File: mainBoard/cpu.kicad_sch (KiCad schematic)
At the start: 11 parts

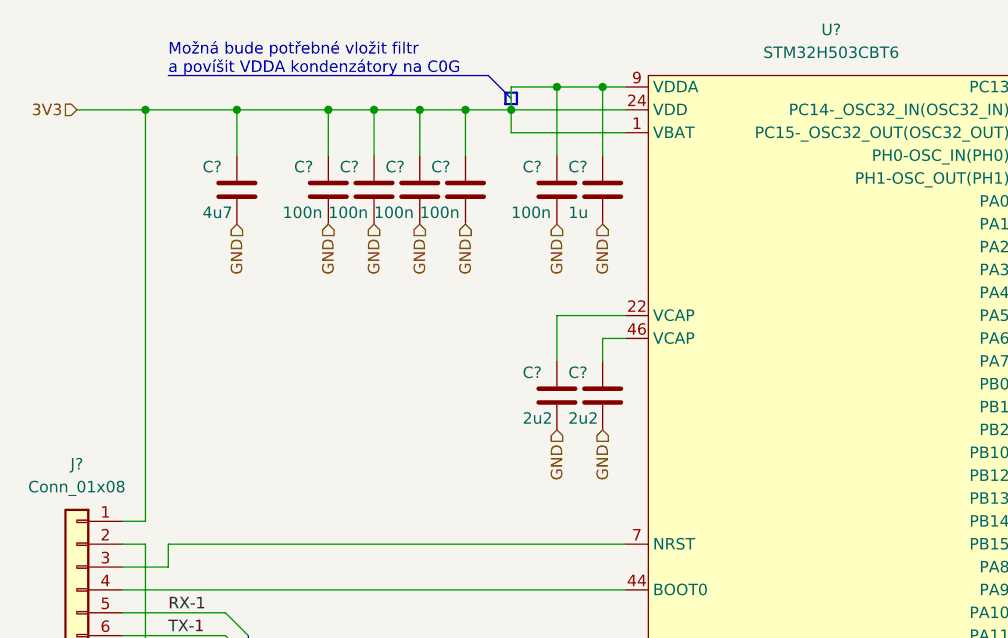
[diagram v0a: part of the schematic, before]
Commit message: LEDky, měření napájení, připojení DRV atd.
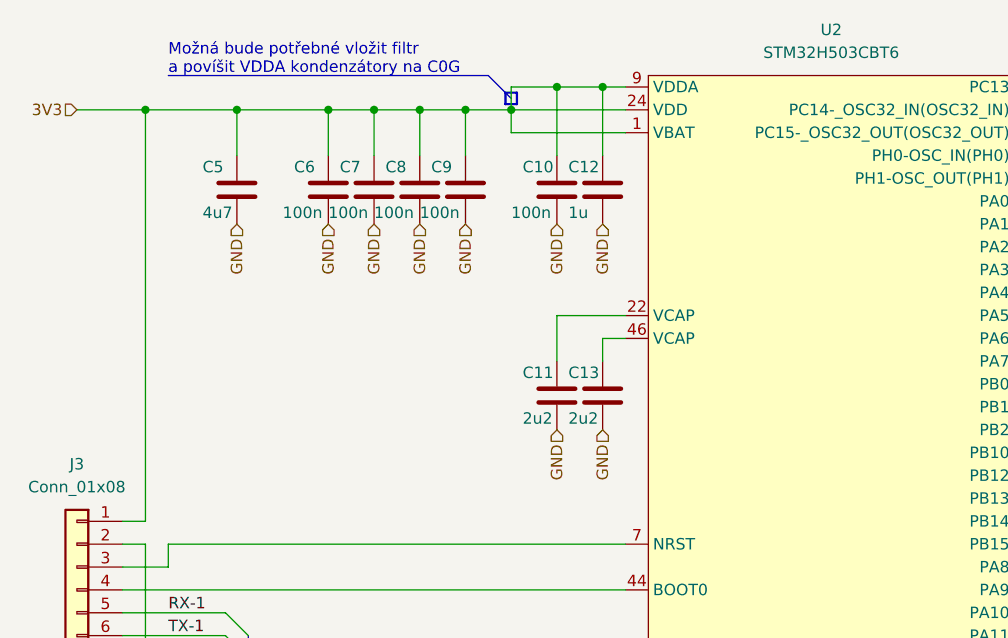
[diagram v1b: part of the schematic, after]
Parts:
- gave numbers to parts that had none: 11

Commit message: Pouzdra
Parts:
- J3: footprint (none) -> Connector_PinHeader_1.00mm:PinHeader_1x08_P1.00mm_Vertical
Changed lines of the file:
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@@
       (effects (font (size 1.27 1.27)))
     )
-    (property "Footprint" "" (at 63.5 100.33 0)
+    (property "Footprint" "Connector_PinHeader_1.00mm:PinHeader_1x08_P1.00mm_Vertical" (at 63.5 100.33 0)
       (effects (font (size 1.27 1.27)) hide)
     )

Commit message: test-pointy a zdvojení konektorů
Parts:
- J3: footprint Connector_PinHeader_1.00mm:PinHeader_1x08_P1.00mm_Vertical -> Connector_JST:JST_XH_B8B-XH-AM_1x08_P2.50mm_Vertical
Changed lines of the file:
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@@
       (effects (font (size 1.27 1.27)))
     )
-    (property "Footprint" "Connector_PinHeader_1.00mm:PinHeader_1x08_P1.00mm_Vertical" (at 63.5 100.33 0)
+    (property "Footprint" "Connector_JST:JST_XH_B8B-XH-AM_1x08_P2.50mm_Vertical" (at 63.5 100.33 0)
       (effects (font (size 1.27 1.27)) hide)
     )

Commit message: WIP
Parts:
- removed J3: Conn_01x08, Connector_JST:JST_XH_B8B-XH-AM_1x08_P2.50mm_Vertical, symbol Connector_Generic:Conn_01x08
- added J10: Conn_02x07_Odd_Even, Connector_PinHeader_1.27mm:PinHeader_2x07_P1.27mm_Vertical_SMD, symbol Connector_Generic:Conn_02x07_Odd_Even
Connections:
- net RX-1: now also J10.13 (Pin_13)
- net SWCLK: now also J10.6 (Pin_6)
- net SWDIO: now also J10.4 (Pin_4)
- net TX-1: now also J10.14 (Pin_14)
- net VDD: now also J10.3 (Pin_3)
- net VSS: now also J10.5 (Pin_5), J10.7 (Pin_7)
- net at U2.7 (NRST): now also J10.12 (Pin_12)
- no-connect marks 0 -> 7
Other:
- moved on the sheet: C10, C11, C12, C13, C5, C6, C7, C8, C9, U2

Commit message: WIP
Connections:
- net DRV-IN1 renamed DRV.IN1
- net DRV-IN2 renamed DRV.IN2
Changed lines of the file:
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@@
 (kicad_sch (version 20230121) (generator eeschema)
   (paper "A4")
+  (junction (at 121.92 43.18) (diameter 0) (color 0 0 0 0)
+  )
   (junction (at 91.44 45.72) (diameter 0) (color 0 0 0 0)
   )
@@
   )
   (junction (at 111.76 45.72) (diameter 0) (color 0 0 0 0)
-  )
-  (junction (at 121.92 43.18) (diameter 0) (color 0 0 0 0)
   )
   (junction (at 106.68 45.72) (diameter 0) (color 0 0 0 0)
@@
     (stroke (width 0) (type default))
   )
-  (bus_entry (at 187.96 93.98) (size 2.54 -2.54)
+  (bus_entry (at 190.5 91.44) (size -2.54 2.54)
     (stroke (width 0) (type default))
   )
@@
     (stroke (width 0) (type default))
   )
+  (wire (pts (xy 170.18 116.84) (xy 196.85 116.84))
+    (stroke (width 0) (type default))
+  )
+  (wire (pts (xy 170.18 109.22) (xy 187.96 109.22))
+    (stroke (width 0) (type default))
+  )
   (bus (pts (xy 190.5 93.98) (xy 190.5 91.44))
     (stroke (width 0) (type default))
@@
     (stroke (width 0) (type default))
   )
-  (wire (pts (xy 170.18 106.68) (xy 187.96 106.68))
-    (stroke (width 0) (type default))
-  )
   (wire (pts (xy 124.46 48.26) (xy 111.76 48.26))
     (stroke (width 0) (type default))
@@
     (stroke (width 0) (type default))
   )
+  (wire (pts (xy 170.18 73.66) (xy 207.01 73.66))
+    (stroke (width 0) (type default))
+  )
   (wire (pts (xy 116.84 68.58) (xy 124.46 68.58))
     (stroke (width 0) (type default))
   )
+  (wire (pts (xy 170.18 114.3) (xy 196.85 114.3))
+    (stroke (width 0) (type default))
+  )
   (bus (pts (xy 190.5 43.18) (xy 190.5 40.64))
     (stroke (width 0) (type default))
@@
     (stroke (width 0) (type default))
   )
-  (wire (pts (xy 170.18 116.84) (xy 196.85 116.84))
+  (wire (pts (xy 170.18 121.92) (xy 196.85 121.92))
+    (stroke (width 0) (type default))
+  )
+  (wire (pts (xy 121.92 43.18) (xy 124.46 43.18))
     (stroke (width 0) (type default))
   )
@@
     (stroke (width 0) (type default))
   )
-  (wire (pts (xy 170.18 127) (xy 201.93 127))
-    (stroke (width 0) (type default))
-  )
   (bus (pts (xy 199.39 50.8) (xy 207.01 50.8))
     (stroke (width 0) (type default))
   )
   (wire (pts (xy 60.96 96.52) (xy 69.85 96.52))
-    (stroke (width 0) (type default))
-  )
-  (wire (pts (xy 207.01 73.66) (xy 170.18 73.66))
-    (stroke (width 0) (type default))
-  )
-  (wire (pts (xy 170.18 119.38) (xy 196.85 119.38))
     (stroke (width 0) (type default))
   )
@@
     (stroke (width 0) (type default))
   )
+  (wire (pts (xy 170.18 127) (xy 201.93 127))
+    (stroke (width 0) (type default))
+  )
   (bus (pts (xy 190.5 43.18) (xy 190.5 78.74))
     (stroke (width 0) (type default))
@@
     (stroke (width 0) (type default))
   )
+  (wire (pts (xy 170.18 106.68) (xy 187.96 106.68))
+    (stroke (width 0) (type default))
+  )
+  (wire (pts (xy 170.18 119.38) (xy 196.85 119.38))
+    (stroke (width 0) (type default))
+  )
+  (wire (pts (xy 170.18 66.04) (xy 201.93 66.04))
+    (stroke (width 0) (type default))
+  )
   (wire (pts (xy 170.18 124.46) (xy 201.93 124.46))
     (stroke (width 0) (type default))
   )
-  (wire (pts (xy 170.18 114.3) (xy 196.85 114.3))
-    (stroke (width 0) (type default))
-  )
-  (wire (pts (xy 170.18 66.04) (xy 201.93 66.04))
-    (stroke (width 0) (type default))
-  )
-  (wire (pts (xy 121.92 43.18) (xy 124.46 43.18))
-    (stroke (width 0) (type default))
-  )
   (wire (pts (xy 63.5 45.72) (xy 67.31 45.72))
+    (stroke (width 0) (type default))
+  )
+  (bus (pts (xy 190.5 88.9) (xy 207.01 88.9))
     (stroke (width 0) (type default))
   )
@@
     (stroke (width 0) (type default))
   )
-  (wire (pts (xy 170.18 109.22) (xy 187.96 109.22))
-    (stroke (width 0) (type default))
-  )
   (wire (pts (xy 67.31 86.36) (xy 67.31 88.9))
     (stroke (width 0) (type default))
@@
     (stroke (width 0) (type default))
   )
-  (bus (pts (xy 190.5 88.9) (xy 207.01 88.9))
-    (stroke (width 0) (type default))
-  )
   (bus (pts (xy 199.39 114.3) (xy 199.39 116.84))
     (stroke (width 0) (type default))
@@
   )
   (bus (pts (xy 204.47 121.92) (xy 204.47 124.46))
-    (stroke (width 0) (type default))
-  )
-  (wire (pts (xy 170.18 121.92) (xy 196.85 121.92))
     (stroke (width 0) (type default))
   )
@@
     (effects (font (size 1.27 1.27)) (justify left bottom))
   )
-  (label "RX-2" (at 170.18 93.98 0) (fields_autoplaced)
+  (label "RX-2" (at 171.45 93.98 0) (fields_autoplaced)
     (effects (font (size 1.27 1.27)) (justify left bottom))
   )
@@
     (effects (font (size 1.27 1.27)) (justify left bottom))
   )
-  (label "DRV-IN1" (at 170.18 127 0) (fields_autoplaced)
+  (label "DRV.IN1" (at 170.18 127 0) (fields_autoplaced)
     (effects (font (size 1.27 1.27)) (justify left bottom))
   )
@@
     (effects (font (size 1.27 1.27)) (justify left bottom))
   )
-  (label "TX-2" (at 170.18 96.52 0) (fields_autoplaced)
+  (label "TX-2" (at 171.45 96.52 0) (fields_autoplaced)
     (effects (font (size 1.27 1.27)) (justify left bottom))
   )
@@
     (effects (font (size 1.27 1.27)) (justify left bottom))
   )
-  (label "DRV-IN2" (at 170.18 124.46 0) (fields_autoplaced)
-    (effects (font (size 1.27 1.27)) (justify left bottom))
-  )
+  (label "DRV.IN2" (at 170.18 124.46 0) (fields_autoplaced)
+    (effects (font (size 1.27 1.27)) (justify left bottom))
+  )

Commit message: ERC
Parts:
- removed U2: STM32H503CBT6, Package_QFP:LQFP-48-1EP_7x7mm_P0.5mm_EP3.6x3.6mm, symbol Robotarna_KiCad_Library:STM32H503CBT6
- added U2: STM32H503CBT6, Package_QFP:LQFP-48-1EP_7x7mm_P0.5mm_EP3.6x3.6mm, symbol RKL-STM:STM32H503CBT6
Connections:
- net DRV.IN1: now also U2.43 (PB7)
- net DRV.IN2: now also U2.42 (PB6)
- net MEŘENÍ-NAPÁJENÍ: now also U2.17 (PA7)
- net RX-1: now also U2.32 (PA11)
- net SWCLK: now also U2.37 (PA14(JTCK/SWCLK))
- net SWDIO: now also U2.34 (PA13(JTMS/SWDIO))
- net TX-1: now also U2.33 (PA12)
- net VDD: now also U2.1 (VBAT), U2.24 (VDD), U2.36 (VDD), U2.48 (VDD), U2.9 (VDDA)
- net VSS: now also U2.23 (VSS), U2.35 (VSS), U2.47 (VSS), U2.8 (VSSA)
- net at C13.1: now also U2.46 (VCAP)
- net at J10.12 (Pin_12): now also U2.7 (NRST)
- net at C11.1: now also U2.22 (VCAP)
- new net DRV.PROUD: U2.13 (PA3)
- new net DRV.VREF: U2.14 (PA4)
- new net ENC.CLK: U2.39 (PB3(JTDO/TRACESWO))
- new net ENC.ENC-TYP-DET: U2.38 (PA15(JTDI))
- new net ENC.MISO: U2.40 (PB4(NJTRST))
- new net ENC.MOSI: U2.41 (PB5)
- new net ENC.POT: U2.10 (PA0)
- new net LED.B: U2.3 (PC14-_OSC32_IN(OSC32_IN))
- new net LED.G: U2.20 (PB2)
- new net LED.R: U2.2 (PC13)
- new net LED.Y: U2.21 (PB10)
- new net UART.RX: U2.28 (PB15)
- new net UART.TX: U2.29 (PA8)
- no-connect marks 7 -> 22

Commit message: WIP
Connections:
- net DRV.IN1: now also U2.42 (PB6); no longer U2.43 (PB7)
- net DRV.IN2: now also U2.43 (PB7); no longer U2.42 (PB6)
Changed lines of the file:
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@@
     (effects (font (size 1.27 1.27)) (justify left bottom))
   )
-  (label "DRV.IN2" (at 170.18 124.46 0)
+  (label "DRV.IN2" (at 170.18 127 0)
     (effects (font (size 1.27 1.27)) (justify left bottom))
   )
-  (label "DRV.IN1" (at 170.18 127 0) (fields_autoplaced)
+  (label "DRV.IN1" (at 170.18 124.46 0) (fields_autoplaced)
     (effects (font (size 1.27 1.27)) (justify left bottom))
   )

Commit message: PCB
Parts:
- added J9: Conn_01x08, Connector_PinHeader_1.00mm:PinHeader_2x04_P1.00mm_Vertical, symbol Connector_Generic:Conn_01x08
- U2: footprint Package_QFP:LQFP-48-1EP_7x7mm_P0.5mm_EP3.6x3.6mm -> Package_QFP:LQFP-48_7x7mm_P0.5mm
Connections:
- net RX-1: now also J9.6 (Pin_6)
- net SWCLK: now also J9.5 (Pin_5)
- net SWDIO: now also J9.3 (Pin_3)
- net TX-1: now also J9.4 (Pin_4)
- net VDD: now also J9.1 (Pin_1)
- net VSS: now also J9.2 (Pin_2), J9.8 (Pin_8)
- net NRST: now reaches J10.12 (Pin_12), U2.7 (NRST)
- net NRST: now also J9.7 (Pin_7)
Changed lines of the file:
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@@
   (junction (at 91.44 45.72) (diameter 0) (color 0 0 0 0)
+  )
+  (junction (at 83.82 142.24) (diameter 0) (color 0 0 0 0)
   )
   (junction (at 116.84 43.18) (diameter 0) (color 0 0 0 0)
@@
     (stroke (width 0) (type default))
   )
+  (bus_entry (at 93.98 142.24) (size -2.54 -2.54)
+    (stroke (width 0) (type default))
+  )
   (bus_entry (at 187.96 106.68) (size 2.54 -2.54)
     (stroke (width 0) (type default))
   )
+  (bus_entry (at 93.98 96.52) (size -2.54 -2.54)
+    (stroke (width 0) (type default))
+  )
+  (bus_entry (at 91.44 132.08) (size 2.54 2.54)
+    (stroke (width 0) (type default))
+  )
   (bus_entry (at 187.96 111.76) (size 2.54 -2.54)
     (stroke (width 0) (type default))
@@
     (stroke (width 0) (type default))
   )
+  (bus_entry (at 91.44 134.62) (size 2.54 2.54)
+    (stroke (width 0) (type default))
+  )
   (bus_entry (at 204.47 121.92) (size -2.54 2.54)
     (stroke (width 0) (type default))
@@
     (stroke (width 0) (type default))
   )
+  (bus_entry (at 91.44 137.16) (size 2.54 2.54)
+    (stroke (width 0) (type default))
+  )
   (bus_entry (at 199.39 114.3) (size -2.54 2.54)
     (stroke (width 0) (type default))
@@
     (stroke (width 0) (type default))
   )
+  (bus_entry (at 91.44 129.54) (size 2.54 2.54)
+    (stroke (width 0) (type default))
+  )
   (bus_entry (at 190.5 93.98) (size -2.54 2.54)
     (stroke (width 0) (type default))
   )
+  (bus_entry (at 93.98 96.52) (size 2.54 -2.54)
+    (stroke (width 0) (type default))
+  )
   (bus (pts (xy 190.5 43.18) (xy 190.5 78.74))
     (stroke (width 0) (type default))
   )
+  (wire (pts (xy 96.52 93.98) (xy 124.46 93.98))
+    (stroke (width 0) (type default))
+  )
   (wire (pts (xy 67.31 88.9) (xy 69.85 88.9))
     (stroke (width 0) (type default))
@@
     (stroke (width 0) (type default))
   )
-  (wire (pts (xy 82.55 93.98) (xy 124.46 93.98))
-    (stroke (width 0) (type default))
-  )
   (wire (pts (xy 124.46 48.26) (xy 111.76 48.26))
     (stroke (width 0) (type default))
@@
     (stroke (width 0) (type default))
   )
+  (bus (pts (xy 93.98 134.62) (xy 93.98 137.16))
+    (stroke (width 0) (type default))
+  )
   (bus (pts (xy 204.47 58.42) (xy 207.01 58.42))
     (stroke (width 0) (type default))
@@
     (stroke (width 0) (type default))
   )
+  (bus (pts (xy 93.98 139.7) (xy 93.98 142.24))
+    (stroke (width 0) (type default))
+  )
+  (wire (pts (xy 83.82 127) (xy 81.28 127))
+    (stroke (width 0) (type default))
+  )
   (wire (pts (xy 170.18 45.72) (xy 187.96 45.72))
     (stroke (width 0) (type default))
@@
   )
   (bus (pts (xy 204.47 58.42) (xy 204.47 60.96))
+    (stroke (width 0) (type default))
+  )
+  (bus (pts (xy 93.98 142.24) (xy 93.98 152.4))
     (stroke (width 0) (type default))
   )
@@
     (stroke (width 0) (type default))
   )
+  (wire (pts (xy 82.55 93.98) (xy 91.44 93.98))
+    (stroke (width 0) (type default))
+  )
   (wire (pts (xy 69.85 83.82) (xy 67.31 83.82))
     (stroke (width 0) (type default))
@@
     (stroke (width 0) (type default))
   )
+  (wire (pts (xy 83.82 142.24) (xy 83.82 127))
+    (stroke (width 0) (type default))
+  )
   (wire (pts (xy 106.68 45.72) (xy 111.76 45.72))
     (stroke (width 0) (type default))
@@
     (stroke (width 0) (type default))
   )
+  (wire (pts (xy 91.44 139.7) (xy 81.28 139.7))
+    (stroke (width 0) (type default))
+  )
   (wire (pts (xy 63.5 45.72) (xy 67.31 45.72))
     (stroke (width 0) (type default))
@@
   )
   (wire (pts (xy 91.44 45.72) (xy 96.52 45.72))
+    (stroke (width 0) (type default))
+  )
+  (wire (pts (xy 81.28 134.62) (xy 91.44 134.62))
     (stroke (width 0) (type default))
   )
@@
     (stroke (width 0) (type default))
   )
-  (bus (pts (xy 93.98 114.3) (xy 93.98 152.4))
+  (bus (pts (xy 93.98 114.3) (xy 93.98 132.08))
+    (stroke (width 0) (type default))
+  )
+  (wire (pts (xy 81.28 129.54) (xy 91.44 129.54))
     (stroke (width 0) (type default))
   )
@@
   )
   (wire (pts (xy 121.92 43.18) (xy 121.92 50.8))
+    (stroke (width 0) (type default))
+  )
+  (wire (pts (xy 81.28 142.24) (xy 83.82 142.24))
+    (stroke (width 0) (type default))
+  )
+  (bus (pts (xy 93.98 96.52) (xy 93.98 99.06))
     (stroke (width 0) (type default))
   )
@@
     (stroke (width 0) (type default))
   )
+  (wire (pts (xy 83.82 144.78) (xy 83.82 142.24))
+    (stroke (width 0) (type default))
+  )
   (wire (pts (xy 69.85 86.36) (xy 67.31 86.36))
     (stroke (width 0) (type default))
@@
     (stroke (width 0) (type default))
   )
+  (wire (pts (xy 81.28 132.08) (xy 91.44 132.08))
+    (stroke (width 0) (type default))
+  )
   (wire (pts (xy 111.76 48.26) (xy 111.76 45.72))
     (stroke (width 0) (type default))
@@
     (stroke (width 0) (type default))
   )
-  (bus (pts (xy 93.98 88.9) (xy 93.98 99.06))
+  (bus (pts (xy 93.98 88.9) (xy 93.98 96.52))
     (stroke (width 0) (type default))
   )
@@
     (stroke (width 0) (type default))
   )
+  (bus (pts (xy 93.98 137.16) (xy 93.98 139.7))
+    (stroke (width 0) (type default))
+  )
   (bus (pts (xy 58.42 114.3) (xy 93.98 114.3))
     (stroke (width 0) (type default))
@@
   )
   (bus (pts (xy 190.5 101.6) (xy 190.5 104.14))
+    (stroke (width 0) (type default))
+  )
+  (wire (pts (xy 81.28 137.16) (xy 91.44 137.16))
+    (stroke (width 0) (type default))
+  )
+  (bus (pts (xy 93.98 132.08) (xy 93.98 134.62))
     (stroke (width 0) (type default))
   )
@@
     (effects (font (size 1.27 1.27)) (justify left bottom))
   )
-  (label "{TX-1 RX-1 SWDIO SWCLK}" (at 127 152.4 0) (fields_autoplaced)
+  (label "{TX-1 RX-1 SWDIO SWCLK NRST}" (at 127 152.4 0) (fields_autoplaced)
     (effects (font (size 1.27 1.27)) (justify left bottom))
   )
@@
     (effects (font (size 1.27 1.27)) (justify left bottom))
   )
+  (label "RX-1" (at 85.09 137.16 0) (fields_autoplaced)
+    (effects (font (size 1.27 1.27)) (justify left bottom))
+  )
+  (label "NRST" (at 96.52 93.98 0)
+    (effects (font (size 1.27 1.27)) (justify left bottom))
+  )
   (label "ENC.MOSI" (at 170.18 121.92 0)
     (effects (font (size 1.27 1.27)) (justify left bottom))
@@
   )
   (label "DRV.IN2" (at 170.18 127 0)
+    (effects (font (size 1.27 1.27)) (justify left bottom))
+  )
+  (label "SWCLK" (at 85.09 134.62 0) (fields_autoplaced)
     (effects (font (size 1.27 1.27)) (justify left bottom))
   )
@@
     (effects (font (size 1.27 1.27)) (justify right bottom))
   )
+  (label "3V3" (at 67.31 45.72 0) (fields_autoplaced)
+    (effects (font (size 1.27 1.27)) (justify left bottom))
+  )
   (label "TX-1" (at 170.18 106.68 0) (fields_autoplaced)
     (effects (font (size 1.27 1.27)) (justify left bottom))
   )
+  (label "NRST" (at 85.09 139.7 0)
+    (effects (font (size 1.27 1.27)) (justify left bottom))
+  )
   (label "SWDIO" (at 85.09 83.82 0) (fields_autoplaced)
     (effects (font (size 1.27 1.27)) (justify left bottom))
@@
     (effects (font (size 1.27 1.27)) (justify left bottom))
   )
+  (label "3V3" (at 81.28 124.46 0) (fields_autoplaced)
+    (effects (font (size 1.27 1.27)) (justify left bottom))
+  )
   (label "RX-1" (at 170.18 104.14 0) (fields_autoplaced)
     (effects (font (size 1.27 1.27)) (justify left bottom))
@@
     (effects (font (size 1.27 1.27)) (justify left bottom))
   )
+  (label "NRST" (at 85.09 93.98 0)
+    (effects (font (size 1.27 1.27)) (justify left bottom))
+  )
   (label "LED.Y" (at 170.18 83.82 0)
     (effects (font (size 1.27 1.27)) (justify left bottom))
   )
+  (label "SWDIO" (at 85.09 129.54 0) (fields_autoplaced)
+    (effects (font (size 1.27 1.27)) (justify left bottom))
+  )
   (label "DRV.PROUD" (at 170.18 63.5 0)
     (effects (font (size 1.27 1.27)) (justify left bottom))
@@
     (effects (font (size 1.27 1.27)) (justify left bottom))
   )
+  (label "TX-1" (at 85.09 132.08 0) (fields_autoplaced)
+    (effects (font (size 1.27 1.27)) (justify left bottom))
+  )
   (hierarchical_label "GND" (shape input) (at 96.52 58.42 270) (fields_autoplaced)
     (effects (font (size 1.27 1.27)) (justify right))
@@
   )
   (hierarchical_label "GND" (shape input) (at 67.31 100.33 270) (fields_autoplaced)
+    (effects (font (size 1.27 1.27)) (justify right))
+  )
+  (hierarchical_label "GND" (shape input) (at 83.82 144.78 270) (fields_autoplaced)
     (effects (font (size 1.27 1.27)) (justify right))
   )
@@
       (effects (font (size 1.27 1.27)))
     )
-    (property "Footprint" "Package_QFP:LQFP-48-1EP_7x7mm_P0.5mm_EP3.6x3.6mm" (at 147.32 35.56 0)
+    (property "Footprint" "Package_QFP:LQFP-48_7x7mm_P0.5mm" (at 147.32 35.56 0)
       (effects (font (size 1.27 1.27)) hide)
     )
@@
         )
       )
+    )
+  )
+  (symbol (lib_id "Connector_Generic:Conn_01x08") (at 76.2 132.08 0) (mirror y) (unit 1)
+    (in_bom yes) (on_board yes) (dnp no) (fields_autoplaced)
+    (property "Reference" "J9" (at 76.2 118.11 0)
+      (effects (font (size 1.27 1.27)))
+    )
+    (property "Value" "Conn_01x08" (at 76.2 120.65 0)
+      (effects (font (size 1.27 1.27)))
+    )
+    (property "Footprint" "Connector_PinHeader_1.00mm:PinHeader_2x04_P1.00mm_Vertical" (at 76.2 132.08 0)
+      (effects (font (size 1.27 1.27)) hide)
+    )
+    (property "Datasheet" "~" (at 76.2 132.08 0)
+      (effects (font (size 1.27 1.27)) hide)
+    )
+    (pin "1")
+    (pin "2")
+    (pin "3")
+    (pin "4")
+    (pin "5")
+    (pin "6")
+    (pin "7")
+    (pin "8")
+    (instances
+      (project "mainBoard"
+        (path "/30ed06d7-0b03-4878-b461-066cda7e7438/b14c8b1b-493a-4a02-90ea-b228e228c2ae"
+          (reference "J9") (unit 1)
+        )
+      )
